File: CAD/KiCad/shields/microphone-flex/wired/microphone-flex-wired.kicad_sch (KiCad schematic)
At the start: 22 parts, among them J1 GND / +5V / OUT, J2 LEFT / 1x05 RIGHT ANGLE, J3 RIGHT / 1x05 RIGHT ANGLE, M1 UP / ONE MODULE ONLY

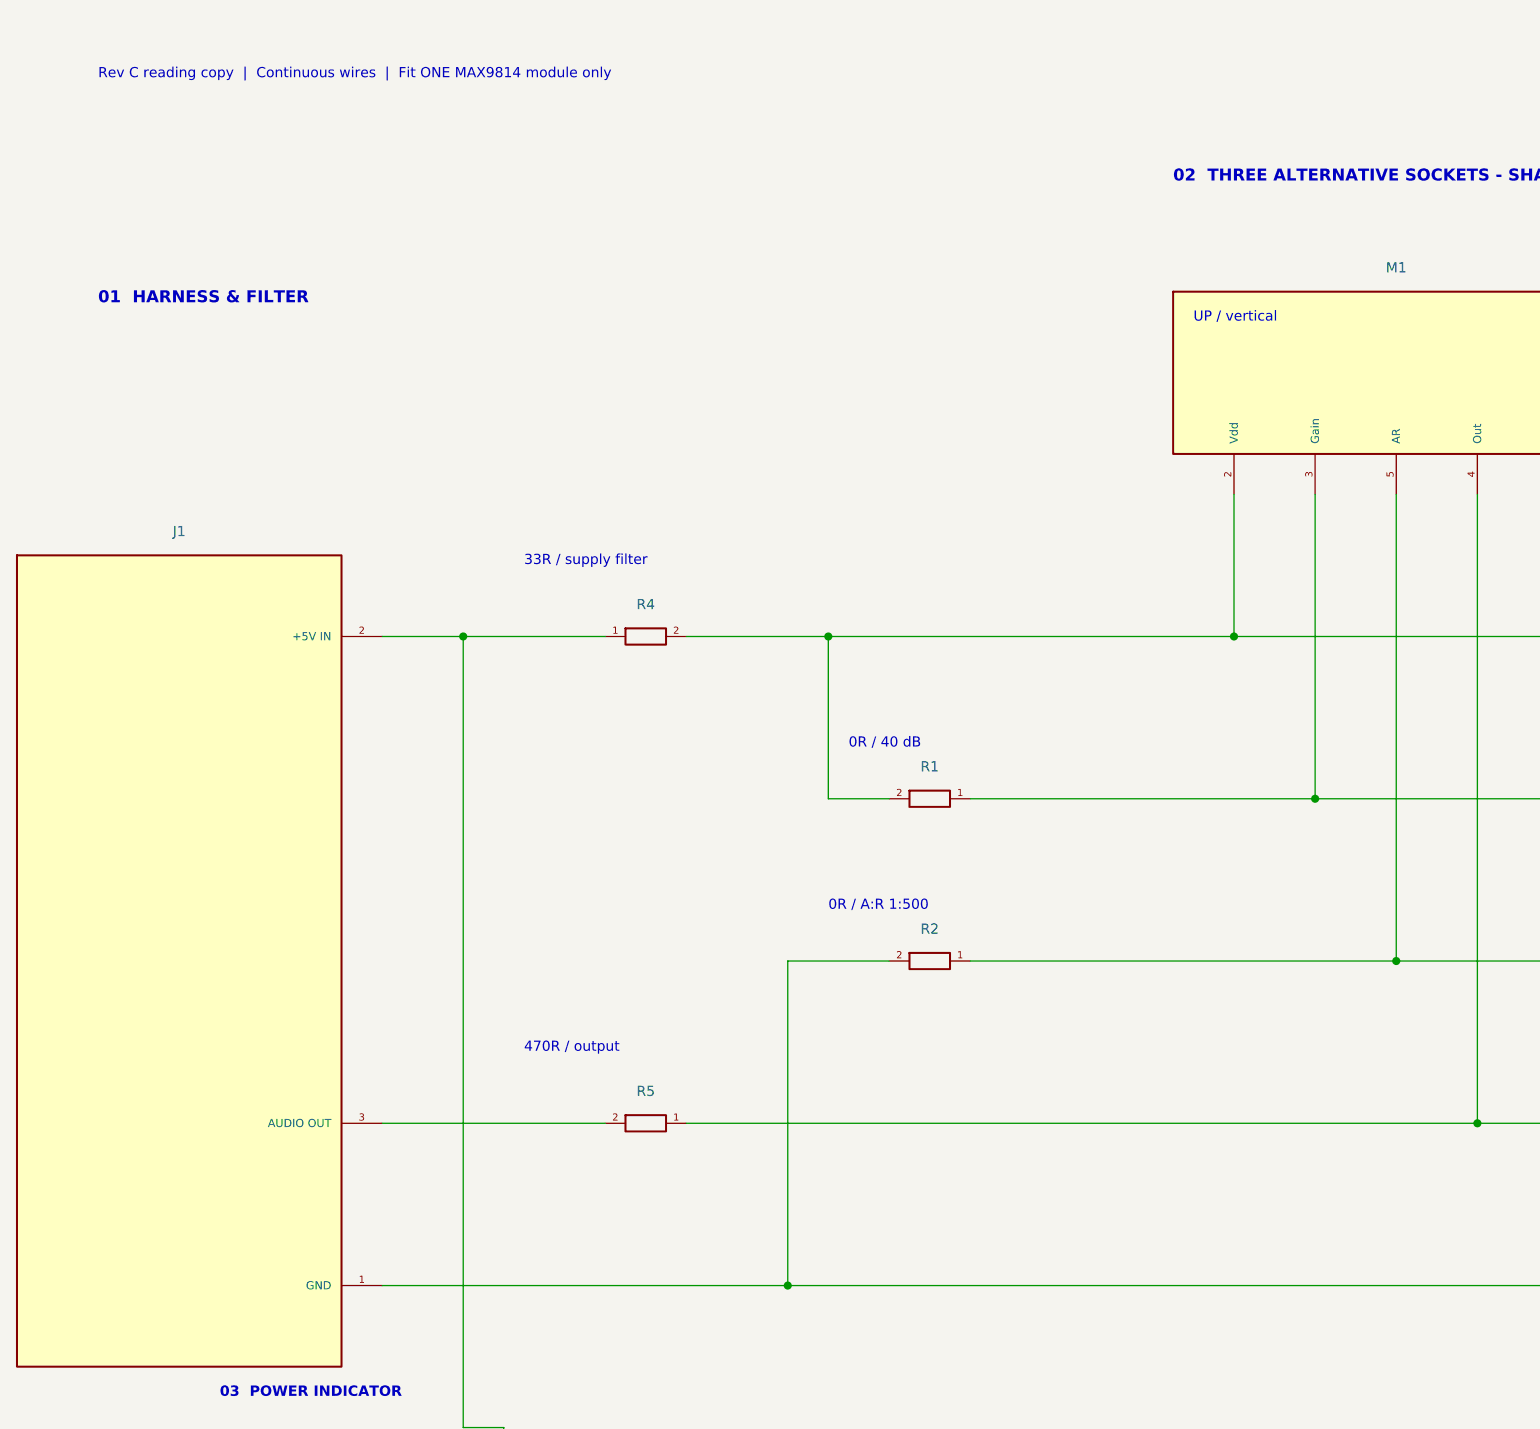
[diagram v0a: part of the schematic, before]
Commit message: Restore removable microphone gain and A/R selectors across flex design
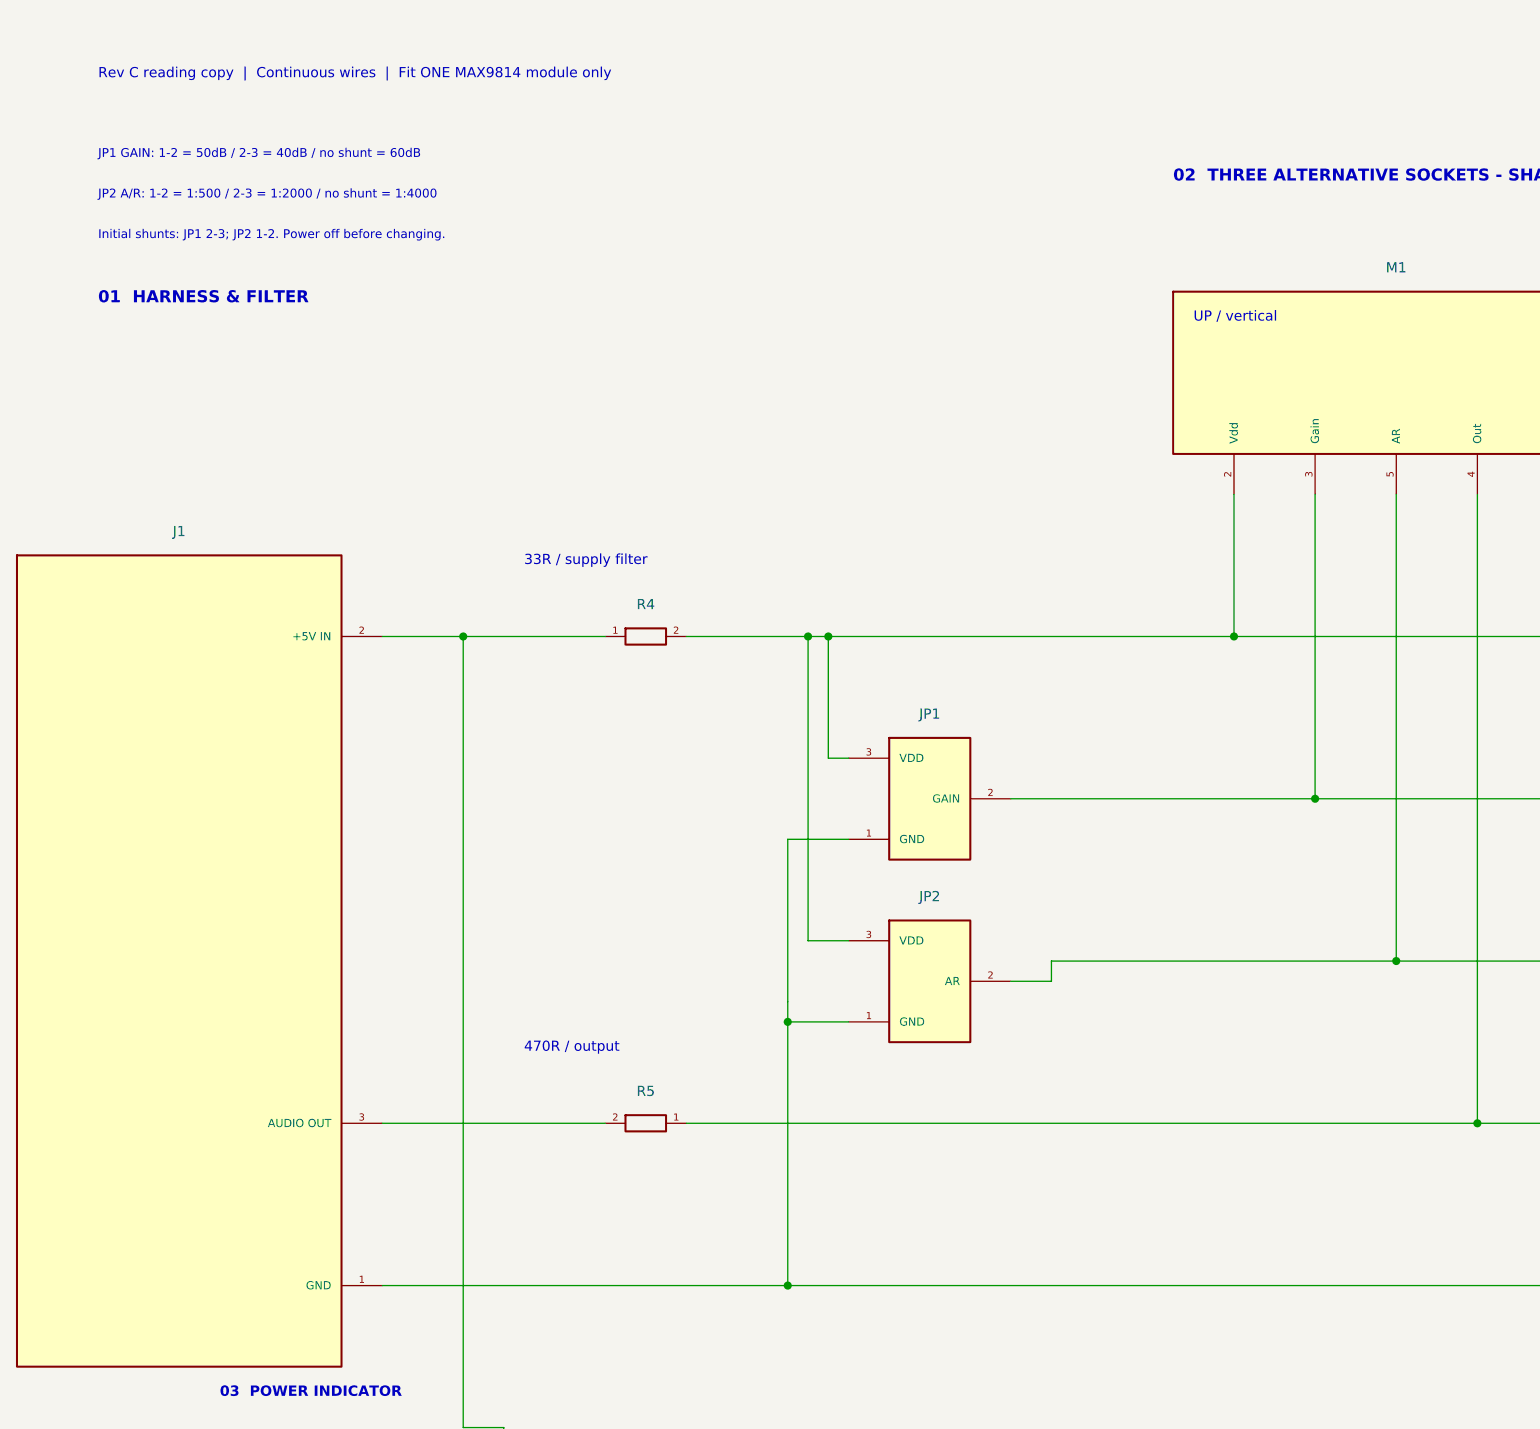
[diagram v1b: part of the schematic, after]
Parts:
- removed R1: 0R / GAIN VDD 40dB, Shields:R_0603_1608Metric, symbol Colloquy:R1
- removed R2: 0R / AR GND 1:500, Shields:R_0603_1608Metric, symbol Colloquy:R2
- added JP1: GAIN SELECT / HEADER + SHUNT, Shields:Flex_Gain_Selector, symbol Colloquy:JP1
- added JP2: AR SELECT / HEADER + SHUNT, Shields:Flex_AR_Selector, symbol Colloquy:JP2
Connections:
- net at C6.1, C7.1, J2.4 (VDD)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: now also JP1.3 (VDD), JP2.3 (VDD)
- net at C6.2, C7.2, D1.1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: now also JP1.1 (GND), JP2.1 (GND)
- net at J2.3 (GAIN), J3.3 (GAIN), M1.3 (Gain): now also JP1.2 (GAIN)
- net at J2.1 (AR), J3.1 (AR), M1.5 (AR): now also JP2.2 (AR)
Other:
- note added: "Initial shunts: JP1 2-3; JP2 1-2. Power off before changing."
- note added: "JP1 GAIN: 1-2 = 50dB / 2-3 = 40dB / no shunt = 60dB"
- note added: "JP2 A/R: 1-2 = 1:500 / 2-3 = 1:2000 / no shunt = 1:4000"
- note removed: "0R / 40 dB"
- note removed: "0R / A:R 1:500"
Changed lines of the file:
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@@
 (kicad_sch (version 20250114) (generator "eeschema") (generator_version "9.0")
  (paper "A3")
-          (title_block (title "Microphone flex - continuous wiring") (date "2026-10-20") (rev "C-wired")
+          (title_block (title "Microphone flex - continuous wiring") (date "2026-10-20") (rev "C-J wired")
             (company "Colloquy of Mobiles") (comment 1 "Electrical reading copy - original PCB and schematic retained"))
           (text "MICROPHONE FLEX / WIRED SCHEMATIC" (at 20.32 17.78 0) (effects (font (size 2.3 2.3) (bold yes)) (justify left top)))
 (text "Rev C reading copy  |  Continuous wires  |  Fit ONE MAX9814 module only" (at 20.32 30.48 0) (effects (font (size 1.27 1.27) ) (justify left top)))
+(text "JP1 GAIN: 1-2 = 50dB / 2-3 = 40dB / no shunt = 60dB" (at 20.32 40.64 0) (effects (font (size 1.1 1.1) ) (justify left top)))
+(text "JP2 A/R: 1-2 = 1:500 / 2-3 = 1:2000 / no shunt = 1:4000" (at 20.32 45.72 0) (effects (font (size 1.1 1.1) ) (justify left top)))
+(text "Initial shunts: JP1 2-3; JP2 1-2. Power off before changing." (at 20.32 50.8 0) (effects (font (size 1.1 1.1) ) (justify left top)))
 (text "01  HARNESS & FILTER" (at 20.32 58.42 0) (effects (font (size 1.5 1.5) (bold yes)) (justify left top)))
 (text "02  THREE ALTERNATIVE SOCKETS - SHARED SIGNALS" (at 154.94 43.18 0) (effects (font (size 1.5 1.5) (bold yes)) (justify left top)))
@@
 (symbol (lib_id "Colloquy:R5") (at 88.9 162.56 0) (unit 1) (in_bom yes) (on_board yes)(property "Reference" "R5" (at 88.9000 158.5440 0) (effects (font (size 1.27 1.27))  ))(property "Value" "470R" (at 88.9000 162.5600 0) (effects (font (size 1.27 1.27))  (hide yes)))(property "Footprint" "Shields:R_0603_1608Metric" (at 88.9000 162.5600 0) (effects (font (size 1.27 1.27))  (hide yes)))(instances (project "microphone-flex-wired" (path "/cd62561b-1660-5a82-97f3-9afdea717d34" (reference "R5") (unit 1)))))
 (text "470R / output" (at 73.66 152.4 0) (effects (font (size 1.27 1.27) ) (justify left top)))
-(symbol (lib_id "Colloquy:R1") (at 124.46000000000001 121.92 0) (unit 1) (in_bom yes) (on_board yes)(property "Reference" "R1" (at 124.4600 117.9040 0) (effects (font (size 1.27 1.27))  ))(property "Value" "0R / GAIN VDD 40dB" (at 124.4600 121.9200 0) (effects (font (size 1.27 1.27))  (hide yes)))(property "Footprint" "Shields:R_0603_1608Metric" (at 124.4600 121.9200 0) (effects (font (size 1.27 1.27))  (hide yes)))(instances (project "microphone-flex-wired" (path "/cd62561b-1660-5a82-97f3-9afdea717d34" (reference "R1") (unit 1)))))
-(text "0R / 40 dB" (at 114.3 114.3 0) (effects (font (size 1.27 1.27) ) (justify left top)))
-(symbol (lib_id "Colloquy:R2") (at 124.46000000000001 142.24 0) (unit 1) (in_bom yes) (on_board yes)(property "Reference" "R2" (at 124.4600 138.2240 0) (effects (font (size 1.27 1.27))  ))(property "Value" "0R / AR GND 1:500" (at 124.4600 142.2400 0) (effects (font (size 1.27 1.27))  (hide yes)))(property "Footprint" "Shields:R_0603_1608Metric" (at 124.4600 142.2400 0) (effects (font (size 1.27 1.27))  (hide yes)))(instances (project "microphone-flex-wired" (path "/cd62561b-1660-5a82-97f3-9afdea717d34" (reference "R2") (unit 1)))))
-(text "0R / A:R 1:500" (at 111.76 134.62 0) (effects (font (size 1.27 1.27) ) (justify left top)))
+(symbol (lib_id "Colloquy:JP1") (at 124.46000000000001 121.92 0) (unit 1) (in_bom yes) (on_board yes)(property "Reference" "JP1" (at 124.4600 111.3000 0) (effects (font (size 1.27 1.27))  ))(property "Value" "GAIN SELECT / HEADER + SHUNT" (at 124.4600 121.9200 0) (effects (font (size 1.27 1.27))  (hide yes)))(property "Footprint" "Shields:Flex_Gain_Selector" (at 124.4600 121.9200 0) (effects (font (size 1.27 1.27))  (hide yes)))(instances (project "microphone-flex-wired" (path "/cd62561b-1660-5a82-97f3-9afdea717d34" (reference "JP1") (unit 1)))))
+(symbol (lib_id "Colloquy:JP2") (at 124.46000000000001 144.78 0) (unit 1) (in_bom yes) (on_board yes)(property "Reference" "JP2" (at 124.4600 134.1600 0) (effects (font (size 1.27 1.27))  ))(property "Value" "AR SELECT / HEADER + SHUNT" (at 124.4600 144.7800 0) (effects (font (size 1.27 1.27))  (hide yes)))(property "Footprint" "Shields:Flex_AR_Selector" (at 124.4600 144.7800 0) (effects (font (size 1.27 1.27))  (hide yes)))(instances (project "microphone-flex-wired" (path "/cd62561b-1660-5a82-97f3-9afdea717d34" (reference "JP2") (unit 1)))))
 (text "03  POWER INDICATOR" (at 35.56 195.58 0) (effects (font (size 1.3 1.3) (bold yes)) (justify left top)))
 (symbol (lib_id "Colloquy:R6") (at 71.12 210.82 0) (unit 1) (in_bom yes) (on_board yes)(property "Reference" "R6" (at 78.7400 208.2800 0) (effects (font (size 1.27 1.27))  ))(property "Value" "2K2" (at 71.1200 210.8200 0) (effects (font (size 1.27 1.27))  (hide yes)))(property "Footprint" "Shields:R_0603_1608Metric" (at 71.1200 210.8200 0) (effects (font (size 1.27 1.27))  (hide yes)))(instances (project "microphone-flex-wired" (path "/cd62561b-1660-5a82-97f3-9afdea717d34" (reference "R6") (unit 1)))))
@@
 (wire (pts (xy 71.1200 238.7600) (xy 71.1200 248.9200)) (stroke (width 0) (type default)))
 (wire (pts (xy 71.1200 248.9200) (xy 233.6800 248.9200)) (stroke (width 0) (type default)))
-(wire (pts (xy 93.9800 101.6000) (xy 111.7600 101.6000)) (stroke (width 0) (type default)))
+(wire (pts (xy 93.9800 101.6000) (xy 109.2200 101.6000)) (stroke (width 0) (type default)))
 (wire (pts (xy 93.9800 162.5600) (xy 193.0400 162.5600)) (stroke (width 0) (type default)))
-(wire (pts (xy 106.6800 142.2400) (xy 106.6800 182.8800)) (stroke (width 0) (type default)))
-(wire (pts (xy 106.6800 142.2400) (xy 119.3800 142.2400)) (stroke (width 0) (type default)))
+(wire (pts (xy 106.6800 127.0000) (xy 106.6800 147.3200)) (stroke (width 0) (type default)))
+(wire (pts (xy 106.6800 127.0000) (xy 114.3000 127.0000)) (stroke (width 0) (type default)))
+(wire (pts (xy 106.6800 147.3200) (xy 106.6800 149.8600)) (stroke (width 0) (type default)))
+(wire (pts (xy 106.6800 149.8600) (xy 106.6800 182.8800)) (stroke (width 0) (type default)))
+(wire (pts (xy 106.6800 149.8600) (xy 114.3000 149.8600)) (stroke (width 0) (type default)))
 (wire (pts (xy 106.6800 182.8800) (xy 203.2000 182.8800)) (stroke (width 0) (type default)))
-(wire (pts (xy 111.7600 101.6000) (xy 111.7600 121.9200)) (stroke (width 0) (type default)))
+(wire (pts (xy 109.2200 101.6000) (xy 109.2200 139.7000)) (stroke (width 0) (type default)))
+(wire (pts (xy 109.2200 101.6000) (xy 111.7600 101.6000)) (stroke (width 0) (type default)))
+(wire (pts (xy 109.2200 139.7000) (xy 114.3000 139.7000)) (stroke (width 0) (type default)))
+(wire (pts (xy 111.7600 101.6000) (xy 111.7600 116.8400)) (stroke (width 0) (type default)))
 (wire (pts (xy 111.7600 101.6000) (xy 162.5600 101.6000)) (stroke (width 0) (type default)))
-(wire (pts (xy 111.7600 121.9200) (xy 119.3800 121.9200)) (stroke (width 0) (type default)))
-(wire (pts (xy 129.5400 121.9200) (xy 172.7200 121.9200)) (stroke (width 0) (type default)))
-(wire (pts (xy 129.5400 142.2400) (xy 182.8800 142.2400)) (stroke (width 0) (type default)))
+(wire (pts (xy 111.7600 116.8400) (xy 114.3000 116.8400)) (stroke (width 0) (type default)))
+(wire (pts (xy 134.6200 121.9200) (xy 172.7200 121.9200)) (stroke (width 0) (type default)))
+(wire (pts (xy 134.6200 144.7800) (xy 139.7000 144.7800)) (stroke (width 0) (type default)))
+(wire (pts (xy 139.7000 142.2400) (xy 139.7000 144.7800)) (stroke (width 0) (type default)))
+(wire (pts (xy 139.7000 142.2400) (xy 182.8800 142.2400)) (stroke (width 0) (type default)))
 (wire (pts (xy 162.5600 83.8200) (xy 162.5600 101.6000)) (stroke (width 0) (type default)))
 (wire (pts (xy 162.5600 101.6000) (xy 233.6800 101.6000)) (stroke (width 0) (type default)))
@@
 (junction (at 106.68 182.88) (diameter 1.016) (color 0 0 0 0))
 (junction (at 233.68 248.92000000000002) (diameter 1.016) (color 0 0 0 0))
+(junction (at 109.22 101.6) (diameter 1.016) (color 0 0 0 0))
+(junction (at 193.04 162.56) (diameter 1.016) (color 0 0 0 0))
+(junction (at 106.68 149.86) (diameter 1.016) (color 0 0 0 0))
+(junction (at 203.2 182.88) (diameter 1.016) (color 0 0 0 0))
 (junction (at 111.76 101.6) (diameter 1.016) (color 0 0 0 0))
-(junction (at 193.04 162.56) (diameter 1.016) (color 0 0 0 0))
-(junction (at 203.2 182.88) (diameter 1.016) (color 0 0 0 0))
 (junction (at 162.56 101.6) (diameter 1.016) (color 0 0 0 0))
 (junction (at 172.72 121.92) (diameter 1.016) (color 0 0 0 0))
